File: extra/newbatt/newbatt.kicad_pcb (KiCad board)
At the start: 2 copper layers, 139 x 45 mm, 33 parts, among them J1 DC050-T, J2 Conn_01x05_MountingPin, U1 BQ24210DQCR, U5 XC6210B332MR

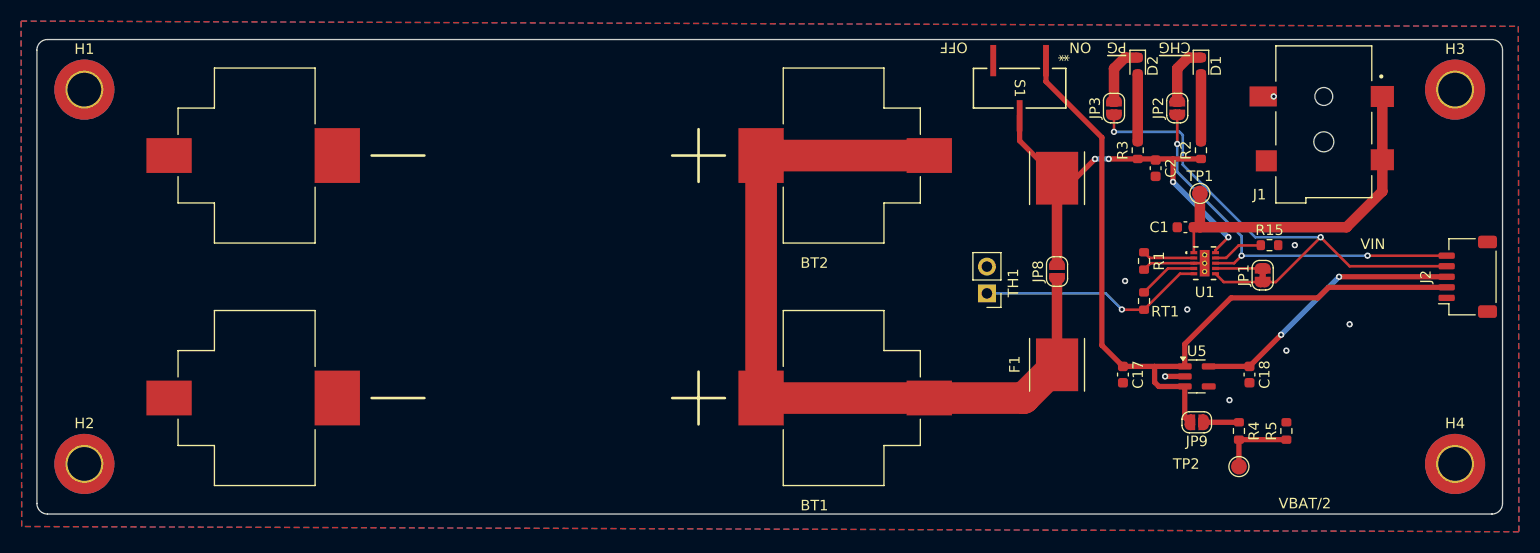
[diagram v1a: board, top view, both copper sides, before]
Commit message: updated battery footprint and slide switch
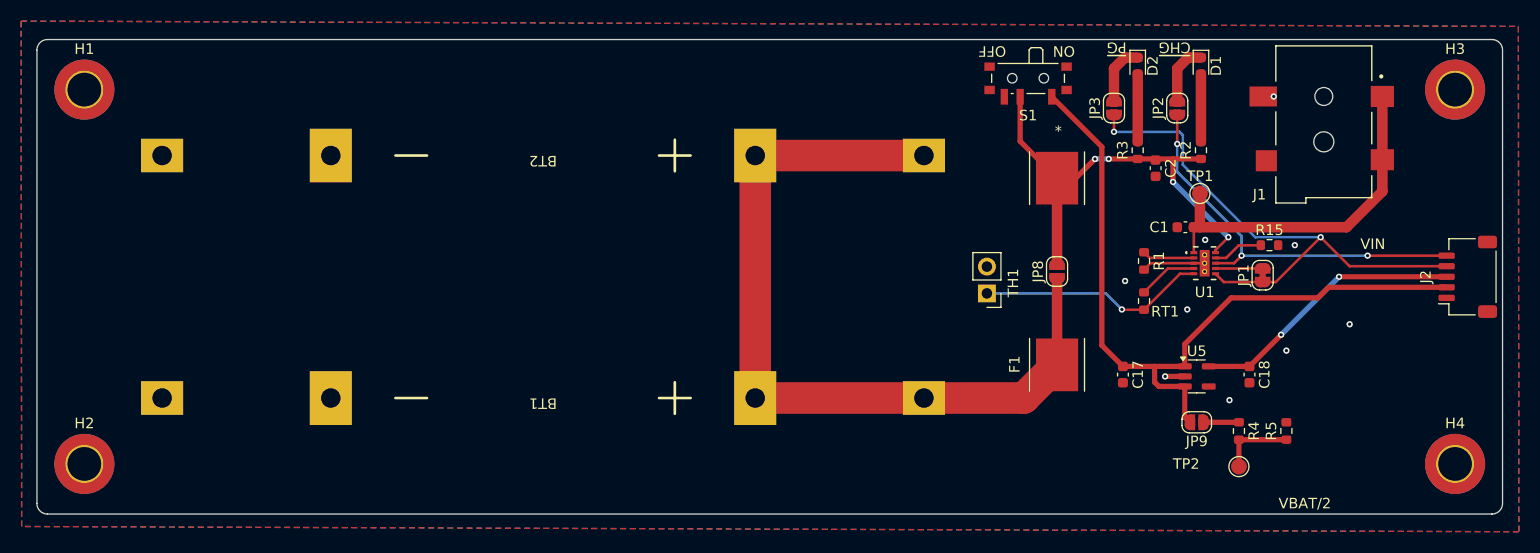
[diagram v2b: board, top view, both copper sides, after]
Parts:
- BT1, BT2: footprint Keystone254TR:BAT_254TR_67mm -> footprints:MY-18650-02
- S1: value JS102011SCQN -> PCM12SMTR; footprint JS102011SCQN:SWITCH_1SCQN -> Button_Switch_SMD:SW_SPDT_PCM12
- moved BT1 20.7 mm to (63.0, 49.0)
- moved BT2 20.7 mm to (63.0, 26.0)
- moved S1 1.01 mm to (109.0, 19.0), turned to 180 degrees
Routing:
- net Net-(J2-Pin_2): track 75.2 -> 71.5 mm
- net Net-(JP8-B): track 41.6 -> 43.3 mm
- net Net-(BT1-+): track 76.5 -> 77.1 mm
- net 0: vias 8 -> 9
